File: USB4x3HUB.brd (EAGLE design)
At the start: 80 x 90 mm, 111 parts, among them IC1 TUSB2036, IC10 SN74LVC1G139DCUR, IC2 FSUSB74MPX, IC6 3.3V, IC7 5V, IC8 5V, IC9 5V, Q1 OSC4_6.0M, SW1 RD, SW2 BL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

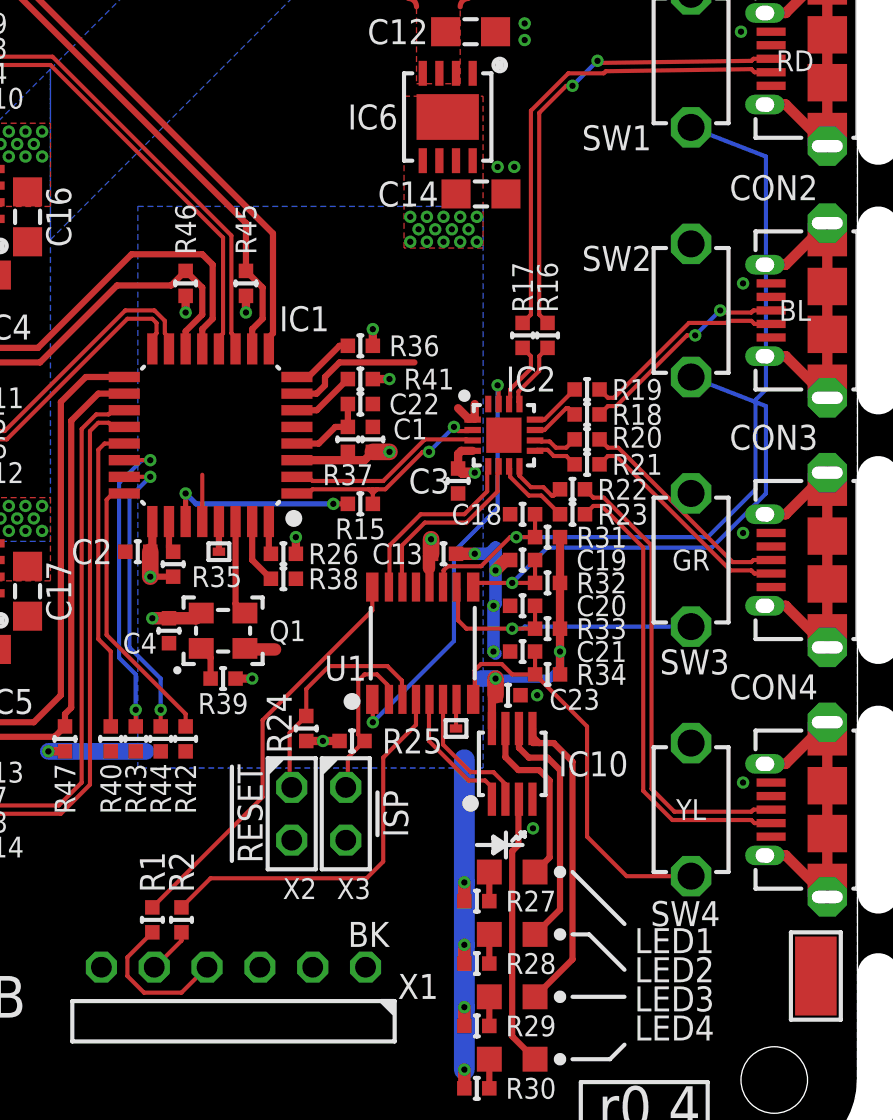
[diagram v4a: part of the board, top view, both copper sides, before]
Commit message: some trace width wider 0.2 -> 0.25mm; Capacotors re-numbering
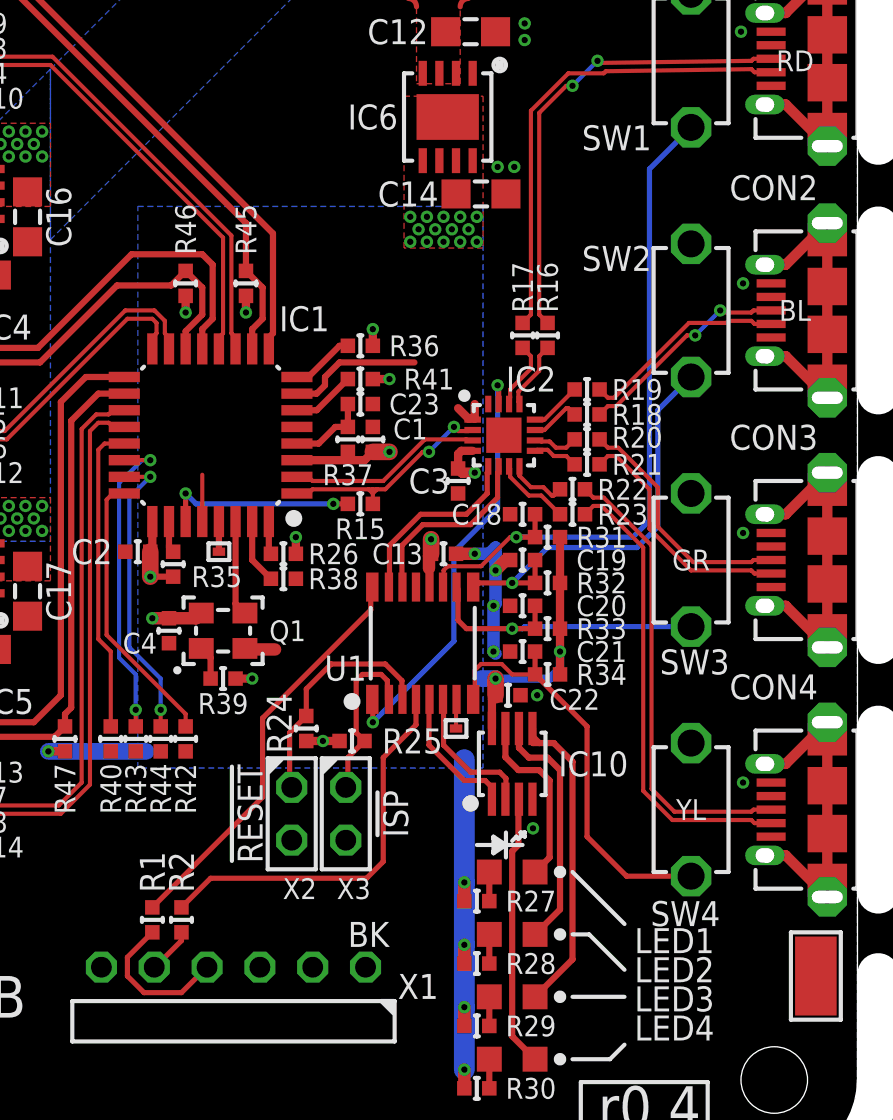
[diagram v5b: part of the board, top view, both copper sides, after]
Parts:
- C22: value 1u/1005 -> (none)
- C23: value (none) -> 1u/1005
- moved C22 15.7 mm to (53.2, 32.5)
- moved C23 15.7 mm to (46.1, 46.5)
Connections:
- net 3.3V: now also C22.1; no longer C23.1
- net N$62: now also C23.1; no longer C22.1
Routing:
- net SW1: track 39.5 -> 33.4 mm
- net SW2: track 26.2 -> 20.2 mm
- net N$9: track 10.8 -> 11.9 mm
- net N$7: track 10.7 -> 11.8 mm

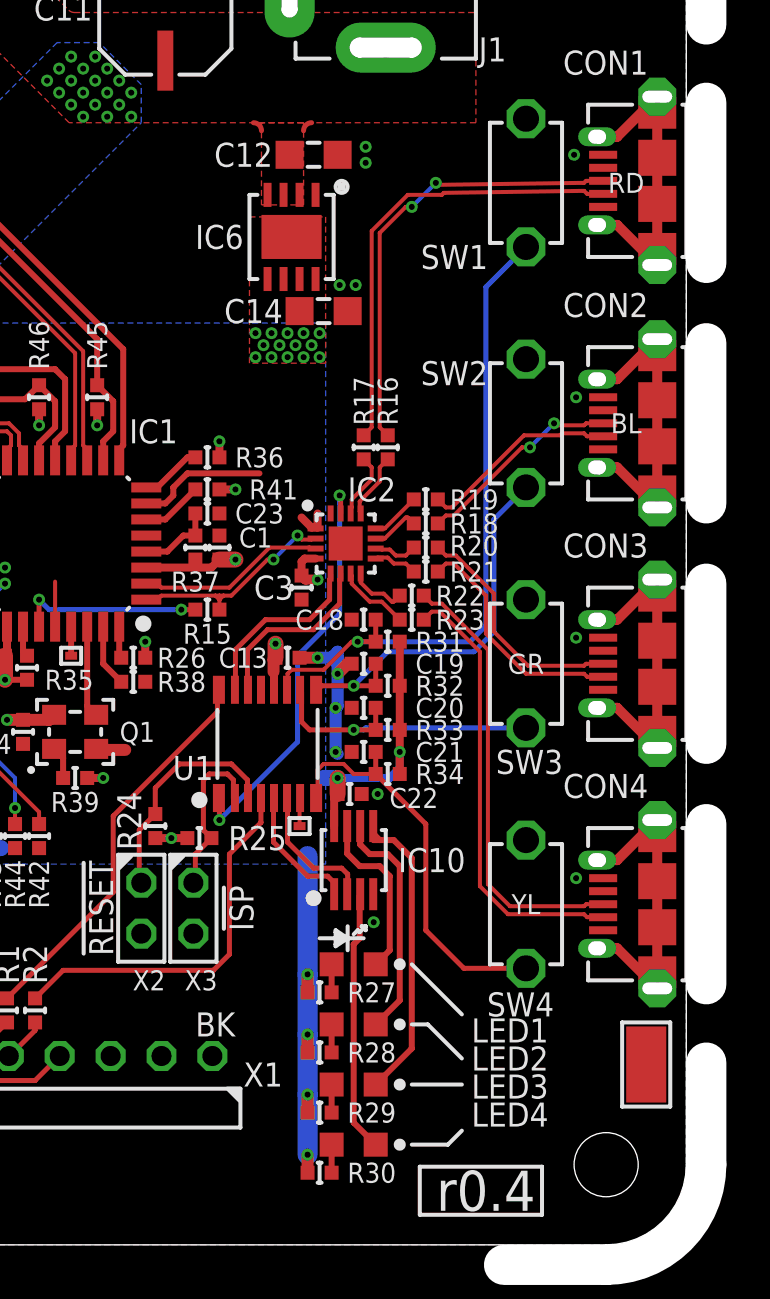
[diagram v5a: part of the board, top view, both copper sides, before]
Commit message: IC6/R16-23,31-34,36,37,41/C1,12,14,18-23 move; LED1-4 colors
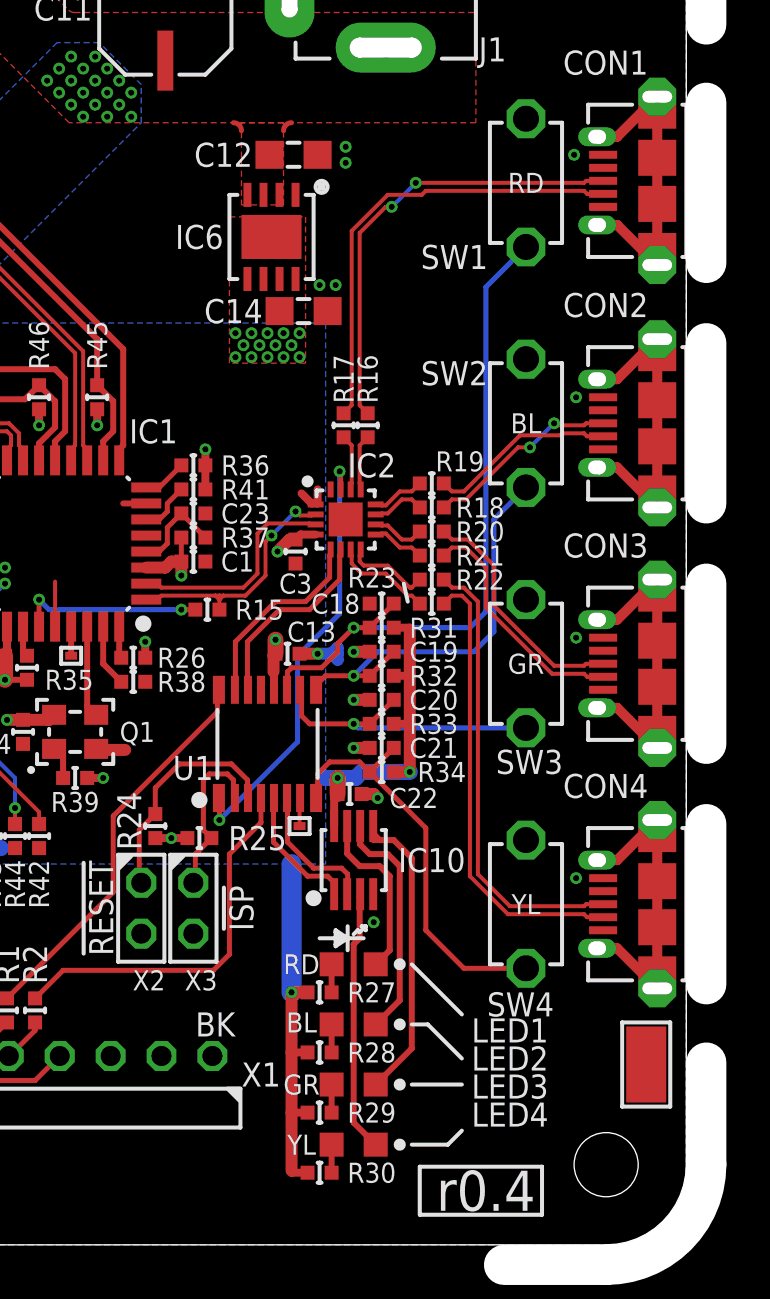
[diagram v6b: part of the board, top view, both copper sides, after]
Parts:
- C10, C11, C8, C9: value C_DENKAI_100U_2.5P6.3_C6 -> 100u/OS-CON
- C12, C14, C15, C16, C17, C5, C6, C7: value (none) -> 4.7u/2012
- C18, C19, C20, C21: value (none) -> 0.1u/1005
- IC3, IC4, IC5: value (none) -> TPS2041C
- Q1: value OSC4_6.0M -> OSC4_48M
- R39: value (none) -> 10k/1005
- moved C3 1.82 mm to (50.5, 44.6)
- moved R16 1.49 mm to (54.1, 50.9)
- moved R17 1.49 mm to (52.9, 50.9)
- moved C1 1.48 mm to (45.4, 44.1), turned to 0 degrees
- moved R22 1.28 mm to (57.3, 43.2)
- moved R23 1.28 mm to (57.3, 42.0)
- moved C18 1.20 mm to (54.8, 42.0)
- moved IC2 1.20 mm to (53.0, 46.2)
- moved C19 1.08 mm to (54.8, 39.6)
- moved C12 1.00 mm to (50.4, 64.4)
- moved C14 1.00 mm to (50.9, 56.6)
- moved IC6 1.00 mm to (49.3, 60.3)
- moved C20 0.98 mm to (54.8, 37.2)
- moved C21 0.92 mm to (54.8, 34.8)
- moved R20 0.85 mm to (57.3, 45.6)
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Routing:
- net GND: track 24.0 -> 16.4 mm
- net 3.3V: track 60.2 -> 63.0 mm, vias 33 -> 29
- net N$2: track 9.38 -> 11.1 mm
- net N$1: track 11.1 -> 12.6 mm
- net N$45: track 2.92 -> 4.32 mm
- net N$49: track 3.67 -> 4.95 mm
- net !OE!: track 20.7 -> 21.9 mm
- net N$61: track 3.07 -> 2.21 mm
- net N$62: track 3.88 -> 4.70 mm
- net SEL1: track 9.07 -> 9.86 mm
- net SEL0: track 9.08 -> 9.82 mm
- net N$6: track 10.0 -> 9.38 mm
- net N$5: track 10.4 -> 9.77 mm
- net N$46: track 3.30 -> 2.79 mm
- net N$42: track 3.30 -> 2.79 mm
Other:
- board text added: "(52,17)"
- board text added: "(52,29)"
- board text added: "(52,41)"
- board text added: "(52,53)"

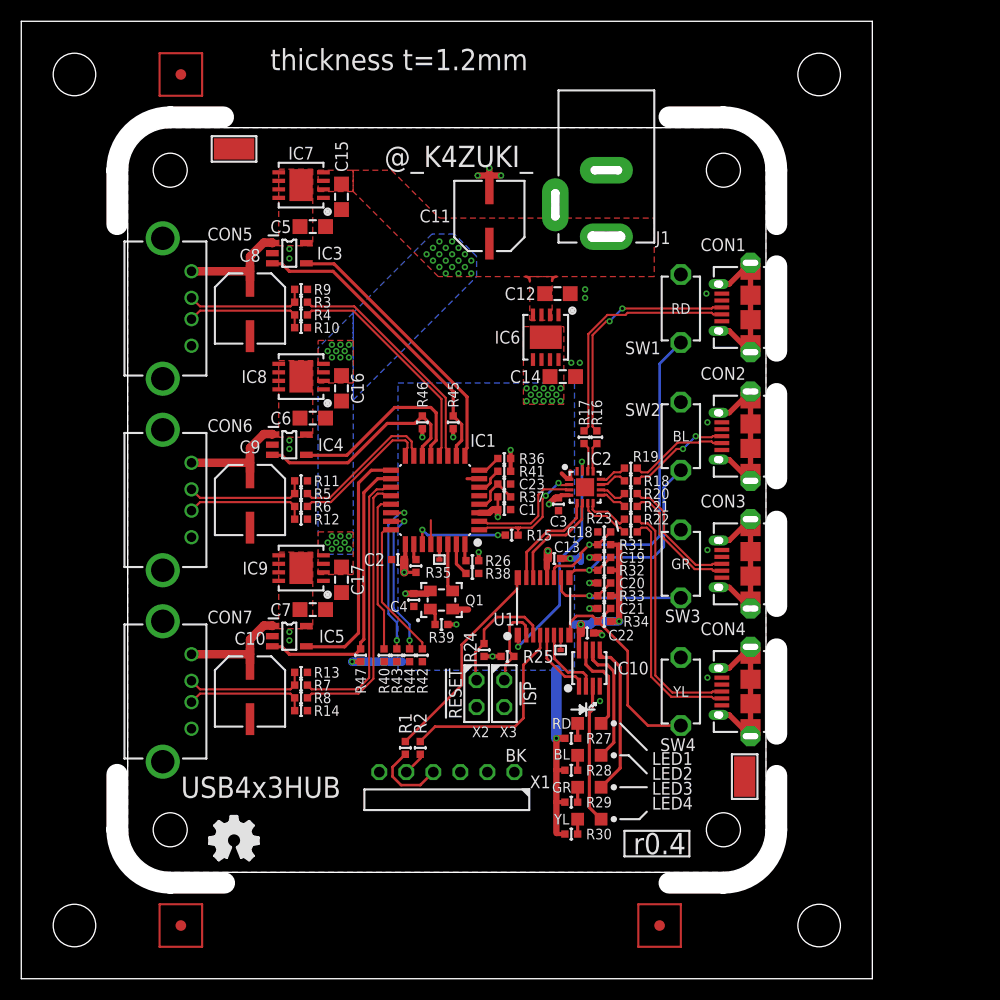
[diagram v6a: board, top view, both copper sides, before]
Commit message: library update; MinLab brand;R15
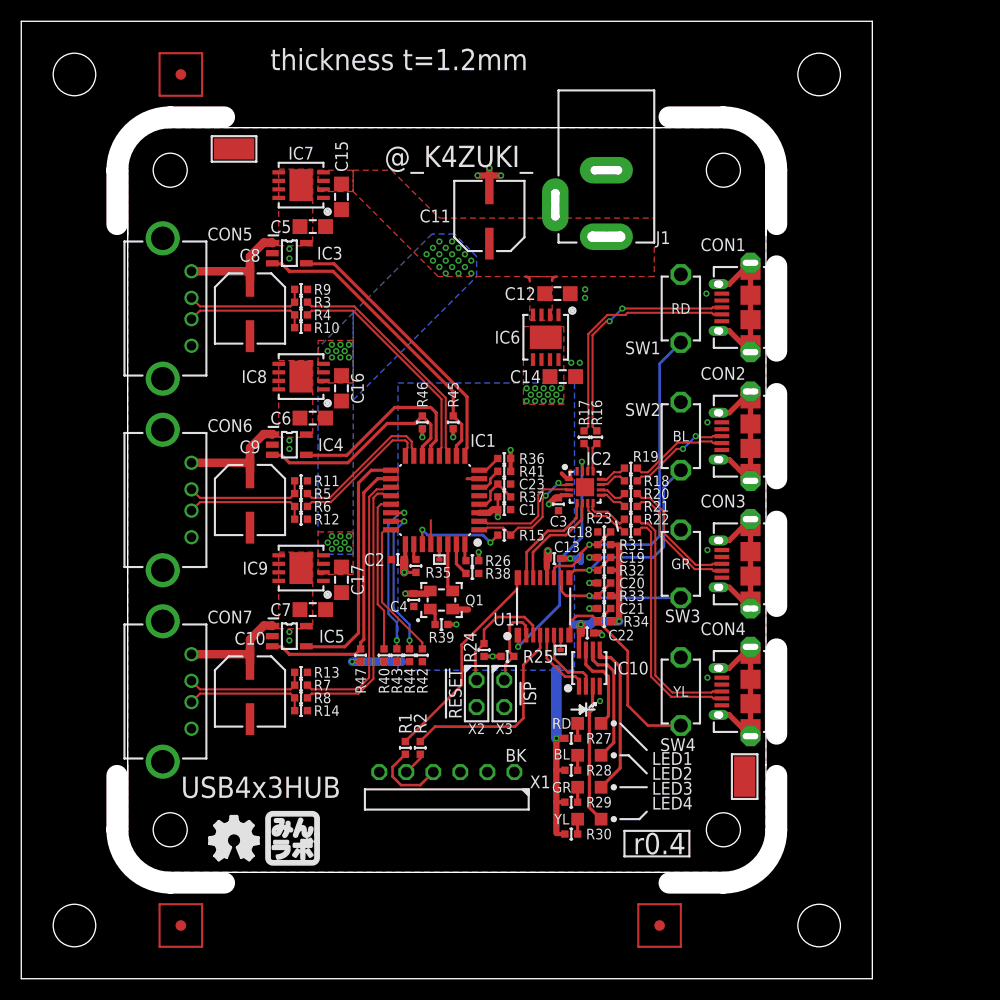
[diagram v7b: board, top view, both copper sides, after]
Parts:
- added I1: (no value), mylib:ICON_MINLAB_5.2MM
- added P1, P2, P3, P4: (no value), mylib:PCB_CORNER
- moved R15 0.70 mm to (45.4, 41.7)
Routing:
- net N$1: track 12.6 -> 12.0 mm
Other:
- outline, holes or cut-outs redrawn

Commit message: [ NEW ] r04 PCB pic
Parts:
- GIT1: value (none) -> 71cae1b
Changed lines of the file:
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@@
 <grid distance="0.1" unitdist="mm" unit="mm" style="dots" multiple="1" display="yes" altdistance="0.025" altunitdist="inch" altunit="inch"/>
 <layers>
-<layer number="1" name="Top" color="12" fill="0" visible="no" active="yes"/>
+<layer number="1" name="Top" color="12" fill="0" visible="yes" active="yes"/>
 <layer number="2" name="Route2" color="1" fill="3" visible="no" active="no"/>
 <layer number="3" name="Route3" color="4" fill="3" visible="no" active="no"/>
 <layer number="14" name="Route14" color="1" fill="6" visible="no" active="no"/>
 <layer number="15" name="Route15" color="4" fill="6" visible="no" active="no"/>
-<layer number="16" name="Bottom" color="9" fill="0" visible="no" active="yes"/>
-<layer number="17" name="Pads" color="2" fill="1" visible="no" active="yes"/>
-<layer number="18" name="Vias" color="2" fill="1" visible="no" active="yes"/>
-<layer number="19" name="Unrouted" color="6" fill="1" visible="no" active="yes"/>
+<layer number="16" name="Bottom" color="9" fill="0" visible="yes" active="yes"/>
+<layer number="17" name="Pads" color="2" fill="1" visible="yes" active="yes"/>
+<layer number="18" name="Vias" color="2" fill="1" visible="yes" active="yes"/>
+<layer number="19" name="Unrouted" color="6" fill="1" visible="yes" active="yes"/>
 <layer number="20" name="Dimension" color="15" fill="1" visible="yes" active="yes"/>
-<layer number="21" name="tPlace" color="7" fill="1" visible="no" active="yes"/>
+<layer number="21" name="tPlace" color="7" fill="1" visible="yes" active="yes"/>
 <layer number="22" name="bPlace" color="7" fill="1" visible="no" active="yes"/>
-<layer number="23" name="tOrigins" color="15" fill="1" visible="no" active="yes"/>
+<layer number="23" name="tOrigins" color="15" fill="1" visible="yes" active="yes"/>
 <layer number="24" name="bOrigins" color="15" fill="1" visible="no" active="yes"/>
-<layer number="25" name="tNames" color="7" fill="1" visible="no" active="yes"/>
+<layer number="25" name="tNames" color="7" fill="1" visible="yes" active="yes"/>
 <layer number="26" name="bNames" color="7" fill="1" visible="no" active="yes"/>
 <layer number="27" name="tValues" color="7" fill="1" visible="no" active="yes"/>
 <layer number="28" name="bValues" color="7" fill="1" visible="no" active="yes"/>
-<layer number="29" name="tStop" color="7" fill="3" visible="no" active="yes"/>
+<layer number="29" name="tStop" color="7" fill="3" visible="yes" active="yes"/>
 <layer number="30" name="bStop" color="7" fill="6" visible="no" active="yes"/>
-<layer number="31" name="tCream" color="7" fill="4" visible="no" active="yes"/>
+<layer number="31" name="tCream" color="7" fill="4" visible="yes" active="yes"/>
 <layer number="32" name="bCream" color="7" fill="5" visible="no" active="yes"/>
 <layer number="33" name="tFinish" color="6" fill="3" visible="no" active="yes"/>
@@
 <layer number="37" name="tTest" color="7" fill="1" visible="no" active="yes"/>
 <layer number="38" name="bTest" color="7" fill="1" visible="no" active="yes"/>
-<layer number="39" name="tKeepout" color="4" fill="11" visible="no" active="yes"/>
+<layer number="39" name="tKeepout" color="4" fill="11" visible="yes" active="yes"/>
 <layer number="40" name="bKeepout" color="1" fill="11" visible="no" active="yes"/>
-<layer number="41" name="tRestrict" color="4" fill="10" visible="no" active="yes"/>
-<layer number="42" name="bRestrict" color="1" fill="10" visible="no" active="yes"/>
-<layer number="43" name="vRestrict" color="2" fill="10" visible="no" active="yes"/>
+<layer number="41" name="tRestrict" color="4" fill="10" visible="yes" active="yes"/>
+<layer number="42" name="bRestrict" color="1" fill="10" visible="yes" active="yes"/>
+<layer number="43" name="vRestrict" color="2" fill="10" visible="yes" active="yes"/>
 <layer number="44" name="Drills" color="7" fill="1" visible="no" active="yes"/>
-<layer number="45" name="Holes" color="7" fill="1" visible="no" active="yes"/>
-<layer number="46" name="Milling" color="3" fill="0" visible="no" active="yes"/>
-<layer number="47" name="Measures" color="7" fill="1" visible="yes" active="yes"/>
+<layer number="45" name="Holes" color="7" fill="1" visible="yes" active="yes"/>
+<layer number="46" name="Milling" color="3" fill="0" visible="yes" active="yes"/>
+<layer number="47" name="Measures" color="7" fill="1" visible="no" active="yes"/>
 <layer number="48" name="Document" color="7" fill="1" visible="no" active="yes"/>
 <layer number="49" name="Reference" color="7" fill="1" visible="no" active="yes"/>
 <layer number="50" name="dxf" color="7" fill="1" visible="no" active="yes"/>
-<layer number="51" name="tDocu" color="7" fill="1" visible="yes" active="yes"/>
+<layer number="51" name="tDocu" color="7" fill="1" visible="no" active="yes"/>
 <layer number="52" name="bDocu" color="7" fill="1" visible="no" active="yes"/>
 <layer number="53" name="tGND_GNDA" color="7" fill="9" visible="no" active="no"/>
@@
 <attribute name="NAME" x="17.5" y="69.4" size="1.2" layer="25" font="vector" ratio="17"/>
 <attribute name="VALUE" x="17.6" y="63.5" size="1.27" layer="27" font="vector" ratio="16" rot="R270"/>
-<attribute name="DIGIKEY" value="" x="16" y="63" size="1.778" layer="27" rot="R270" display="off"/>
+<attribute name="DIGIKEY" value="UE27AC54100-ND" x="16" y="63" size="1.778" layer="27" rot="R270" display="off"/>
 <attribute name="AKIZUKI" value="C-07674" x="16" y="63" size="1.778" layer="27" rot="R270" display="off"/>
 </element>
@@
 <attribute name="NAME" x="17.5" y="51.4" size="1.2" layer="25" font="vector" ratio="17"/>
 <attribute name="VALUE" x="17.6" y="45.5" size="1.27" layer="27" font="vector" ratio="16" rot="R270"/>
-<attribute name="DIGIKEY" value="" x="16" y="45" size="1.778" layer="27" rot="R270" display="off"/>
+<attribute name="DIGIKEY" value="UE27AC54100-ND" x="16" y="45" size="1.778" layer="27" rot="R270" display="off"/>
 <attribute name="AKIZUKI" value="C-07674" x="16" y="45" size="1.778" layer="27" rot="R270" display="off"/>
 </element>
@@
 <attribute name="NAME" x="17.5" y="33.4" size="1.2" layer="25" font="vector" ratio="17"/>
 <attribute name="VALUE" x="17.6" y="27.5" size="1.27" layer="27" font="vector" ratio="16" rot="R270"/>
-<attribute name="DIGIKEY" value="" x="16" y="27" size="1.778" layer="27" rot="R270" display="off"/>
+<attribute name="DIGIKEY" value="UE27AC54100-ND" x="16" y="27" size="1.778" layer="27" rot="R270" display="off"/>
 <attribute name="AKIZUKI" value="C-07674" x="16" y="27" size="1.778" layer="27" rot="R270" display="off"/>
 </element>
@@
 <attribute name="VALUE" x="49.5" y="16.7" size="1" layer="27" ratio="20" rot="R90"/>
 <attribute name="AKIZUKI" value="C-05336" x="40" y="17.9" size="1.778" layer="27" display="off"/>
+<attribute name="DIGIKEY" value="952-2372-ND" x="40" y="17.9" size="1.778" layer="27" display="off"/>
 </element>
 <element name="X2" library="con-samtec.local" package="TSW-102-02-S-S" value="TSW-102-02-S-S" x="42.8" y="26.8" smashed="yes" rot="R90">
@@
 <attribute name="NOT_COMPONENT" value="YES" x="60" y="12.7" size="1.778" layer="27" display="off"/>
 </element>
-<element name="GIT1" library="git-revision" package="GIT-REVISION" value="" x="10" y="10">
+<element name="GIT1" library="git-revision" package="GIT-REVISION" value="71cae1b" x="10" y="10">
 <attribute name="NOT_COMPONENT" value="YES" x="10" y="10" size="1.778" layer="27" display="off"/>
 </element>
@@
 <wire x1="34.9" y1="50.6" x2="36.1" y2="50.6" width="0.2" layer="1"/>
 <wire x1="36.1" y1="50.6" x2="36.3" y2="50.4" width="0.2" layer="1"/>
-<wire x1="36.3" y1="50.4" x2="36.3" y2="49.9" width="0.2" layer="1"/>
+<wire x1="36.3" y1="49.9" x2="36.3" y2="50.4" width="0.2" layer="1"/>
 </signal>
 <signal name="N$39">
